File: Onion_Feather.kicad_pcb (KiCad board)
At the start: 4 copper layers, 59.7 x 53.3 mm, 64 parts, among them IC1 MAX11646EUA+T, J1 HR911105A, J2 CON_HEADER_PRG_AVR_ICSP-PTH, J3 Conn_01x02, J4 USB_A, J5 M04PTH, U1 ONION-OMEGA2, U2 AP1117-33, U3 CP2102N-A01-GQFN24, U4 BQ25895RTW, U5 STF202-22T1G

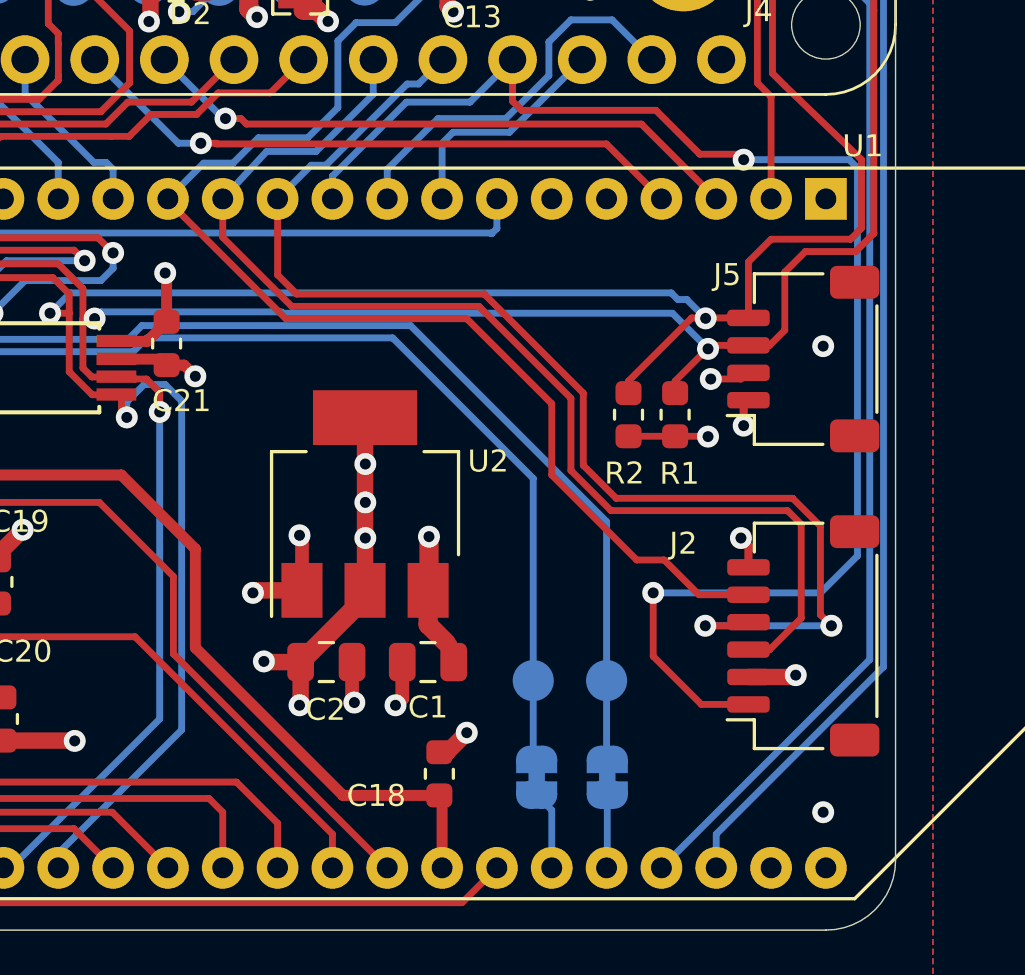
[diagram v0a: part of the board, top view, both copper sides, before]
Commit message: #7 Add tri-state buffer
Signed-off-by: Tisham Dhar <whatnickd@gmail.com>
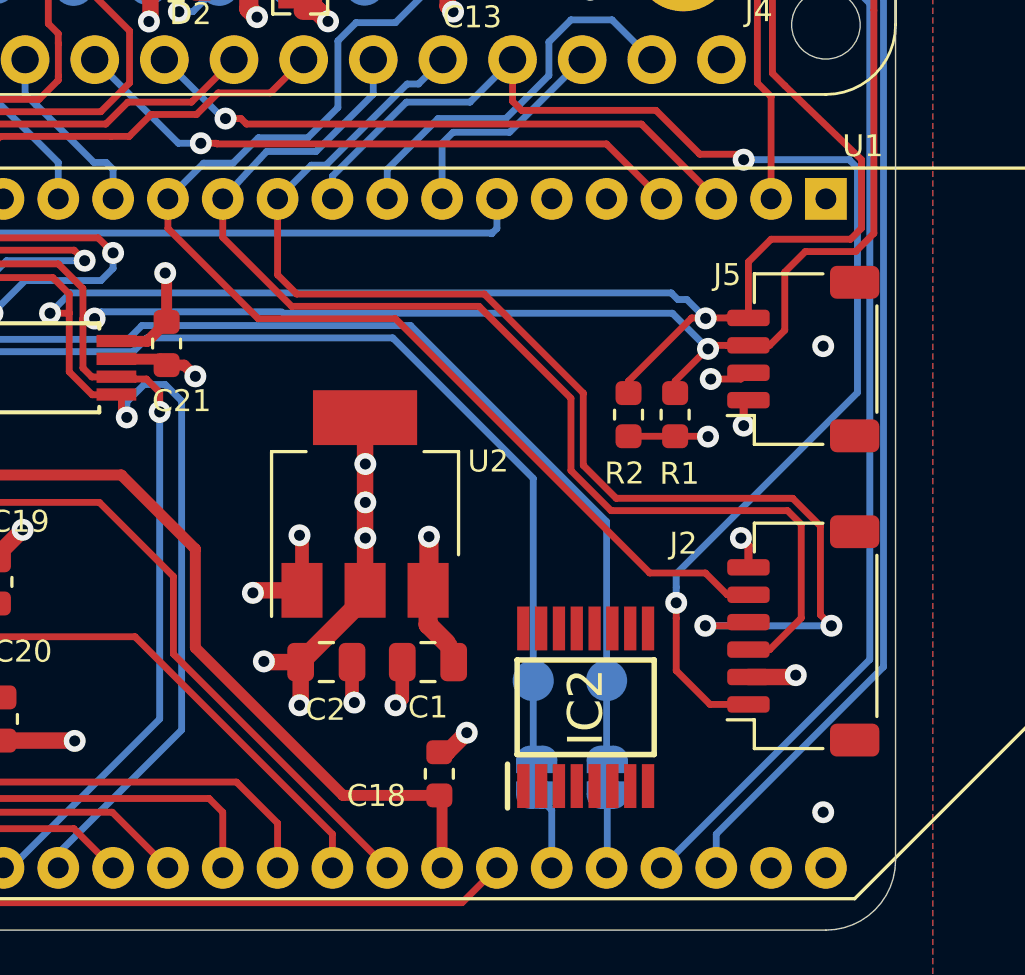
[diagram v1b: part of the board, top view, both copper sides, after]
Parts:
- added IC2: SN74HC367PWR, footprints:SOP65P640X120-16N, F.Cu at (156.3, 106.2)
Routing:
- net MISO: track 52.9 -> 48.5 mm
- net CS: track 61.6 -> 60.7 mm
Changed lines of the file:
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@@
     (tracks 1057)
     (zones 0)
-    (modules 64)
-    (nets 83)
+    (modules 65)
+    (nets 99)
   )
   (page A4)
@@
   (net 81 "Net-(U3-Pad1)")
   (net 82 "/Power Subsystems/V_UPS")
+  (net 83 "Net-(IC2-Pad16)")
+  (net 84 "Net-(IC2-Pad15)")
+  (net 85 "Net-(IC2-Pad14)")
+  (net 86 "Net-(IC2-Pad13)")
+  (net 87 "Net-(IC2-Pad12)")
+  (net 88 "Net-(IC2-Pad11)")
+  (net 89 "Net-(IC2-Pad10)")
+  (net 90 "Net-(IC2-Pad9)")
+  (net 91 "Net-(IC2-Pad8)")
+  (net 92 "Net-(IC2-Pad7)")
+  (net 93 "Net-(IC2-Pad6)")
+  (net 94 "Net-(IC2-Pad5)")
+  (net 95 "Net-(IC2-Pad4)")
+  (net 96 "Net-(IC2-Pad3)")
+  (net 97 "Net-(IC2-Pad2)")
+  (net 98 "Net-(IC2-Pad1)")
   (net_class Default "This is the default net class."
     (clearance 0.2)
@@
     (add_net "Net-(C7-Pad2)")
     (add_net "Net-(IC1-Pad3)")
+    (add_net "Net-(IC2-Pad1)")
+    (add_net "Net-(IC2-Pad10)")
+    (add_net "Net-(IC2-Pad11)")
+    (add_net "Net-(IC2-Pad12)")
+    (add_net "Net-(IC2-Pad13)")
+    (add_net "Net-(IC2-Pad14)")
+    (add_net "Net-(IC2-Pad15)")
+    (add_net "Net-(IC2-Pad16)")
+    (add_net "Net-(IC2-Pad2)")
+    (add_net "Net-(IC2-Pad3)")
+    (add_net "Net-(IC2-Pad4)")
+    (add_net "Net-(IC2-Pad5)")
+    (add_net "Net-(IC2-Pad6)")
+    (add_net "Net-(IC2-Pad7)")
+    (add_net "Net-(IC2-Pad8)")
+    (add_net "Net-(IC2-Pad9)")
     (add_net "Net-(J1-Pad10)")
     (add_net "Net-(J1-Pad11)")
@@
     (add_net ~RESET)
   )
+  (module footprints:SOP65P640X120-16N (layer F.Cu)
+    (at 156.337 106.172 90)
+    (descr TSSOP-PW)
+    (tags "Integrated Circuit")
+    (attr smd)
+    (fp_text reference IC2 (at 0 0 90) (layer F.SilkS)
+      (effects (font (size 1.27 1.27) (thickness 0.254)))
+    )
+    (fp_text value SN74HC367PWR (at 0 0 90) (layer F.SilkS) hide
+      (effects (font (size 1.27 1.27) (thickness 0.254)))
+    )
+    (fp_line (start -3.675 -2.85) (end -2.075 -2.85) (layer F.SilkS) (width 0.2))
+    (fp_line (start -1.725 2.5) (end -1.725 -2.5) (layer F.SilkS) (width 0.2))
+    (fp_line (start 1.725 2.5) (end -1.725 2.5) (layer F.SilkS) (width 0.2))
+    (fp_line (start 1.725 -2.5) (end 1.725 2.5) (layer F.SilkS) (width 0.2))
+    (fp_line (start -1.725 -2.5) (end 1.725 -2.5) (layer F.SilkS) (width 0.2))
+    (fp_line (start -2.2 -1.85) (end -1.55 -2.5) (layer F.Fab) (width 0.1))
+    (fp_line (start -2.2 2.5) (end -2.2 -2.5) (layer F.Fab) (width 0.1))
+    (fp_line (start 2.2 2.5) (end -2.2 2.5) (layer F.Fab) (width 0.1))
+    (fp_line (start 2.2 -2.5) (end 2.2 2.5) (layer F.Fab) (width 0.1))
+    (fp_line (start -2.2 -2.5) (end 2.2 -2.5) (layer F.Fab) (width 0.1))
+    (fp_line (start -3.925 2.8) (end -3.925 -2.8) (layer F.CrtYd) (width 0.05))
+    (fp_line (start 3.925 2.8) (end -3.925 2.8) (layer F.CrtYd) (width 0.05))
+    (fp_line (start 3.925 -2.8) (end 3.925 2.8) (layer F.CrtYd) (width 0.05))
+    (fp_line (start -3.925 -2.8) (end 3.925 -2.8) (layer F.CrtYd) (width 0.05))
+    (fp_text user %R (at 0 0 90) (layer F.Fab)
+      (effects (font (size 1.27 1.27) (thickness 0.254)))
+    )
+    (pad 16 smd rect (at 2.875 -2.275 180) (size 0.45 1.6) (layers F.Cu F.Paste F.Mask)
+      (net 83 "Net-(IC2-Pad16)"))
+    (pad 15 smd rect (at 2.875 -1.625 180) (size 0.45 1.6) (layers F.Cu F.Paste F.Mask)
+      (net 84 "Net-(IC2-Pad15)"))
+    (pad 14 smd rect (at 2.875 -0.975 180) (size 0.45 1.6) (layers F.Cu F.Paste F.Mask)
+      (net 85 "Net-(IC2-Pad14)"))
+    (pad 13 smd rect (at 2.875 -0.325 180) (size 0.45 1.6) (layers F.Cu F.Paste F.Mask)
+      (net 86 "Net-(IC2-Pad13)"))
+    (pad 12 smd rect (at 2.875 0.325 180) (size 0.45 1.6) (layers F.Cu F.Paste F.Mask)
+      (net 87 "Net-(IC2-Pad12)"))
+    (pad 11 smd rect (at 2.875 0.975 180) (size 0.45 1.6) (layers F.Cu F.Paste F.Mask)
+      (net 88 "Net-(IC2-Pad11)"))
+    (pad 10 smd rect (at 2.875 1.625 180) (size 0.45 1.6) (layers F.Cu F.Paste F.Mask)
+      (net 89 "Net-(IC2-Pad10)"))
+    (pad 9 smd rect (at 2.875 2.275 180) (size 0.45 1.6) (layers F.Cu F.Paste F.Mask)
+      (net 90 "Net-(IC2-Pad9)"))
+    (pad 8 smd rect (at -2.875 2.275 180) (size 0.45 1.6) (layers F.Cu F.Paste F.Mask)
+      (net 91 "Net-(IC2-Pad8)"))
+    (pad 7 smd rect (at -2.875 1.625 180) (size 0.45 1.6) (layers F.Cu F.Paste F.Mask)
+      (net 92 "Net-(IC2-Pad7)"))
+    (pad 6 smd rect (at -2.875 0.975 180) (size 0.45 1.6) (layers F.Cu F.Paste F.Mask)
+      (net 93 "Net-(IC2-Pad6)"))
+    (pad 5 smd rect (at -2.875 0.325 180) (size 0.45 1.6) (layers F.Cu F.Paste F.Mask)
+      (net 94 "Net-(IC2-Pad5)"))
+    (pad 4 smd rect (at -2.875 -0.325 180) (size 0.45 1.6) (layers F.Cu F.Paste F.Mask)
+      (net 95 "Net-(IC2-Pad4)"))
+    (pad 3 smd rect (at -2.875 -0.975 180) (size 0.45 1.6) (layers F.Cu F.Paste F.Mask)
+      (net 96 "Net-(IC2-Pad3)"))
+    (pad 2 smd rect (at -2.875 -1.625 180) (size 0.45 1.6) (layers F.Cu F.Paste F.Mask)
+      (net 97 "Net-(IC2-Pad2)"))
+    (pad 1 smd rect (at -2.875 -2.275 180) (size 0.45 1.6) (layers F.Cu F.Paste F.Mask)
+      (net 98 "Net-(IC2-Pad1)"))
+    (model SN74HC367PWR.stp
+      (at (xyz 0 0 0))
+      (scale (xyz 1 1 1))
+      (rotate (xyz 0 0 0))
+    )
+  )
   (module Module:Onion_Omega2+ locked (layer F.Cu)
     (at 165.1 87.63 270)
@@
   (segment (start 160.712653 91.987347) (end 160.025306 91.3) (width 0.25) (layer B.Cu) (net 8))
   (segment (start 160.025306 91.3) (end 159.7 91.3) (width 0.25) (layer B.Cu) (net 8))
-  (segment (start 159.2 100.8) (end 160.4685 102.0685) (width 0.25) (layer F.Cu) (net 9))
-  (segment (start 141.1 87.7) (end 145.4 92) (width 0.25) (layer F.Cu) (net 9) (status 10))
-  (segment (start 160.4685 102.0685) (end 162.2745 102.0685) (width 0.25) (layer F.Cu) (net 9) (status 20))
-  (segment (start 145.4 92) (end 152 92) (width 0.25) (layer F.Cu) (net 9))
-  (segment (start 152 92) (end 155.1 95.1) (width 0.25) (layer F.Cu) (net 9))
-  (segment (start 141.1 87.63) (end 141.1 87.7) (width 0.25) (layer F.Cu) (net 9) (status 30))
-  (segment (start 155.1 95.1) (end 155.1 97.7) (width 0.25) (layer F.Cu) (net 9))
-  (segment (start 158.2 100.8) (end 159.2 100.8) (width 0.25) (layer F.Cu) (net 9))
-  (segment (start 155.1 97.7) (end 158.2 100.8) (width 0.25) (layer F.Cu) (net 9))
   (segment (start 150.871022 64.511022) (end 149.478999 63.118999) (width 0.25) (layer B.Cu) (net 9))
   (segment (start 141.1 87.63) (end 142.404999 86.325001) (width 0.25) (layer B.Cu) (net 9))
@@
   (segment (start 142.404999 86.325001) (end 143.474999 86.325001) (width 0.25) (layer B.Cu) (net 9))
   (segment (start 149.478999 63.118999) (end 148.59 62.23) (width 0.25) (layer B.Cu) (net 9))
+  (segment (start 161.4995 102.0685) (end 162.2745 102.0685) (width 0.25) (layer F.Cu) (net 9))
+  (segment (start 149.4 92) (end 158.674999 101.274999) (width 0.25) (layer F.Cu) (net 9))
+  (segment (start 158.674999 101.274999) (end 160.705999 101.274999) (width 0.25) (layer F.Cu) (net 9))
+  (segment (start 141.1 88.70763) (end 144.39237 92) (width 0.25) (layer F.Cu) (net 9))
+  (segment (start 141.1 87.63) (end 141.1 88.70763) (width 0.25) (layer F.Cu) (net 9))
+  (segment (start 160.705999 101.274999) (end 161.4995 102.0685) (width 0.25) (layer F.Cu) (net 9))
+  (segment (start 144.39237 92) (end 149.4 92) (width 0.25) (layer F.Cu) (net 9))
   (segment (start 152.12 84.1) (end 153.67 82.55) (width 0.25) (layer B.Cu) (net 10) (status 20))
   (segment (start 149.8 84.1) (end 152.12 84.1) (width 0.25) (layer B.Cu) (net 10))
   (segment (start 147.1 86.8) (end 149.8 84.1) (width 0.25) (layer B.Cu) (net 10))
   (segment (start 147.1 87.63) (end 147.1 86.8) (width 0.25) (layer B.Cu) (net 10) (status 10))
-  (segment (start 160.555314 106.0685) (end 158.8 104.313186) (width 0.25) (layer F.Cu) (net 10))
-  (segment (start 162.2745 106.0685) (end 160.555314 106.0685) (width 0.25) (layer F.Cu) (net 10) (status 10))
   (segment (start 153.67 84.07) (end 154 84.4) (width 0.25) (layer F.Cu) (net 10))
   (segment (start 153.67 82.55) (end 153.67 84.07) (width 0.25) (layer F.Cu) (net 10) (status 10))
@@
   (segment (start 160.5 86) (end 161.9 86) (width 0.25) (layer F.Cu) (net 10))
   (segment (start 161.9 86) (end 162.1 86.2) (width 0.25) (layer F.Cu) (net 10))
+  (segment (start 159.639 101.307315) (end 159.639 101.796316) (width 0.25) (layer B.Cu) (net 10))
+  (segment (start 159.639 102.927686) (end 159.639 102.362001) (width 0.25) (layer F.Cu) (net 10))
+  (segment (start 162.2745 106.0685) (end 160.8735 106.0685) (width 0.25) (layer F.Cu) (net 10))
+  (segment (start 159.639 104.834) (end 159.639 102.927686) (width 0.25) (layer F.Cu) (net 10))
+  (segment (start 166.24999 94.696325) (end 159.639 101.307315) (width 0.25) (layer B.Cu) (net 10))
   (segment (start 162.1 86.2) (end 165.94999 86.2) (width 0.25) (layer B.Cu) (net 10))
+  (segment (start 159.639 101.796316) (end 159.639 102.362001) (width 0.25) (layer B.Cu) (net 10))
+  (segment (start 160.8735 106.0685) (end 159.639 104.834) (width 0.25) (layer F.Cu) (net 10))
+  (via (at 159.639 102.362001) (size 0.8) (drill 0.4) (layers F.Cu B.Cu) (net 10))
+  (segment (start 166.24999 86.5) (end 166.24999 94.696325) (width 0.25) (layer B.Cu) (net 10))
   (segment (start 165.94999 86.2) (end 166.24999 86.5) (width 0.25) (layer B.Cu) (net 10))
-  (segment (start 166.24999 86.5) (end 166.24999 100.65001) (width 0.25) (layer B.Cu) (net 10))
-  (segment (start 166.24999 100.65001) (end 164.9 102) (width 0.25) (layer B.Cu) (net 10))
-  (segment (start 164.9 102) (end 158.8 102) (width 0.25) (layer B.Cu) (net 10))
-  (via (at 158.8 102) (size 0.8) (drill 0.4) (layers F.Cu B.Cu) (net 10))
-  (segment (start 158.8 104.313186) (end 158.8 102) (width 0.25) (layer F.Cu) (net 10))
   (segment (start 149.824591 83.438999) (end 150.241001 83.438999) (width 0.25) (layer B.Cu) (net 11))
   (segment (start 150.241001 83.438999) (end 151.13 82.55) (width 0.25) (layer B.Cu) (net 11) (status 20))

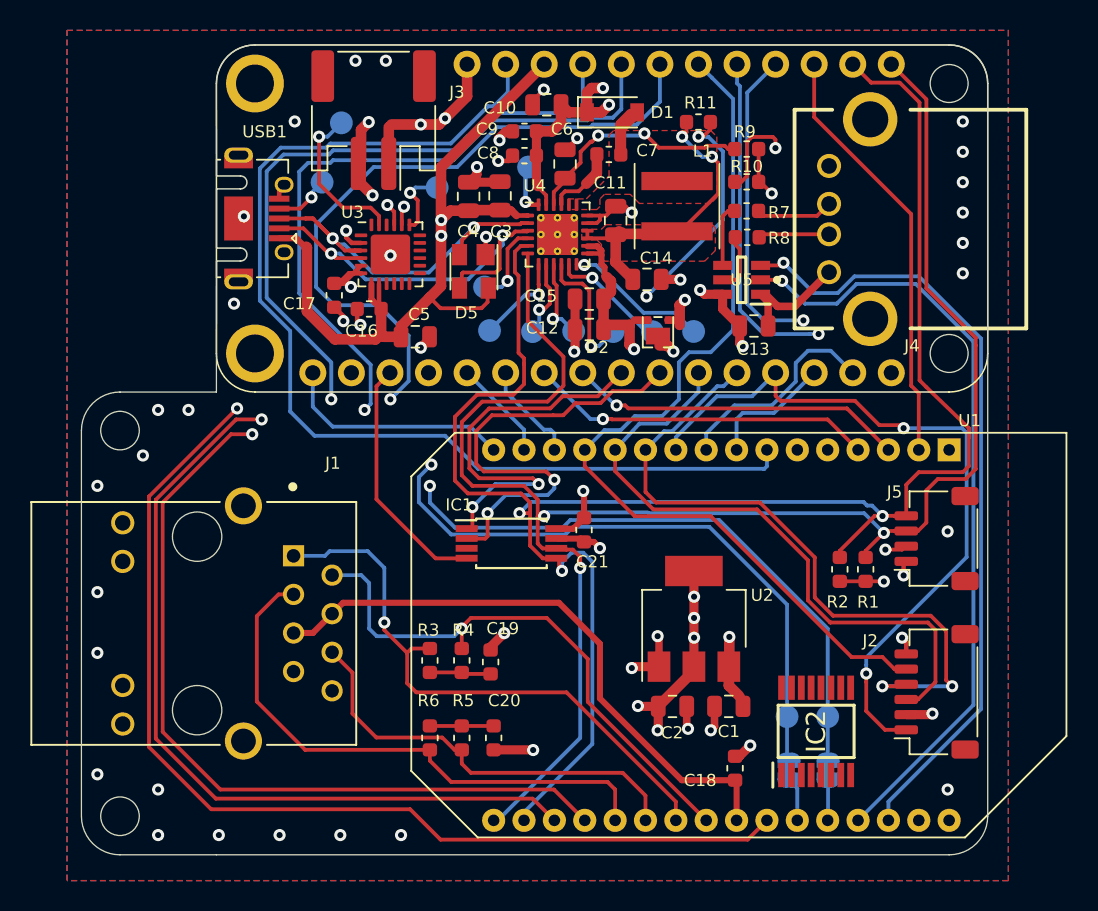
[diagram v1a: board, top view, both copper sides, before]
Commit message: #7 Re-route with tristate buffer
Signed-off-by: Tisham Dhar <whatnickd@gmail.com>
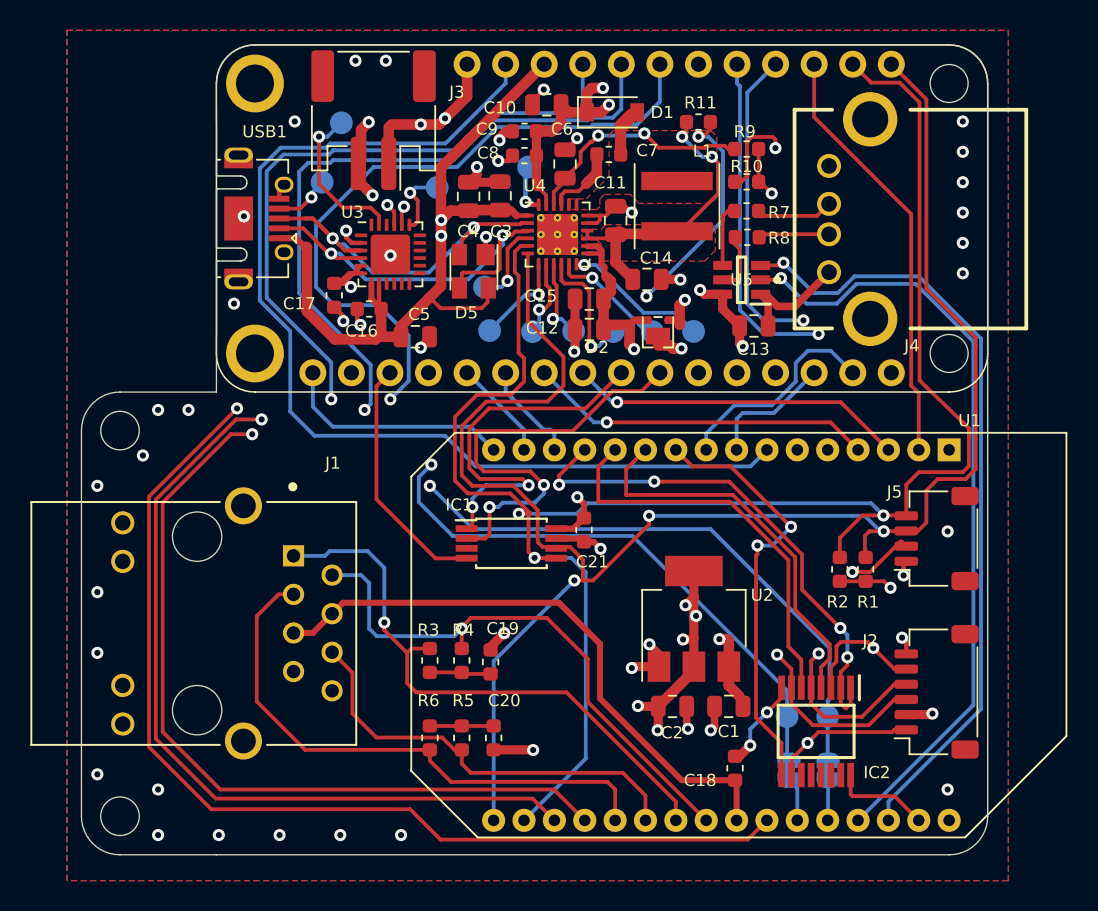
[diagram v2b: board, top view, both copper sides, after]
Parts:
- turned IC2 to 270 degrees
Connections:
- IC2 pad 1: Net-(IC2-Pad1) -> /OnionModule/CS
- IC2 pad 10: Net-(IC2-Pad10) -> MISO_BUF
- IC2 pad 16: Net-(IC2-Pad16) -> 3.3V
- IC2 pad 2: Net-(IC2-Pad2) -> /OnionModule/CS
- IC2 pad 3: Net-(IC2-Pad3) -> CS_BUF
- IC2 pad 4: Net-(IC2-Pad4) -> /OnionModule/MOSI
- IC2 pad 5: Net-(IC2-Pad5) -> MOSI_BUF
- IC2 pad 6: Net-(IC2-Pad6) -> /OnionModule/CLK
- IC2 pad 7: Net-(IC2-Pad7) -> SCLK_BUF
- IC2 pad 8: Net-(IC2-Pad8) -> GND
- IC2 pad 9: Net-(IC2-Pad9) -> /OnionModule/MISO
- J2 pad 1: MISO -> MISO_BUF
- J2 pad 3: SCLK -> SCLK_BUF
- J2 pad 4: MOSI -> MOSI_BUF
- J2 pad 5: CS -> CS_BUF
- MS1 pad 11: SCLK -> SCLK_BUF
- MS1 pad 12: MOSI -> MOSI_BUF
- MS1 pad 13: MISO -> MISO_BUF
- MS1 pad 22: CS -> CS_BUF
- U1 pad 10: MISO -> /OnionModule/MISO
- U1 pad 11: MOSI -> /OnionModule/MOSI
- U1 pad 12: SCLK -> /OnionModule/CLK
- U1 pad 13: CS -> /OnionModule/CS
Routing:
- net CS: track 60.7 -> 0.00 mm
- net SCLK_BUF: track 0.00 -> 59.9 mm, vias 0 -> 1
- net CS_BUF: track 0.00 -> 59.4 mm, vias 0 -> 1
- net MOSI_BUF: track 0.00 -> 48.6 mm, vias 0 -> 1
- net MISO: track 48.5 -> 0.00 mm, vias 2 -> 0
- net MISO_BUF: track 0.00 -> 48.2 mm, vias 0 -> 1
- net MOSI: track 46.1 -> 0.00 mm, vias 2 -> 0
- net SCLK: track 42.6 -> 0.00 mm
- net /OnionModule/CS: track 0.00 -> 34.3 mm, vias 0 -> 4
- net /OnionModule/MISO: track 0.00 -> 28.3 mm, vias 0 -> 2
- net /OnionModule/CLK: track 0.00 -> 26.8 mm
- net /OnionModule/MOSI: track 0.00 -> 26.1 mm
- net 3.3V: track 28.2 -> 39.8 mm
- net GND: track 59.6 -> 64.0 mm, vias 55 -> 56
- net /Power Subsystems/V_UPS: track 56.4 -> 60.5 mm
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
